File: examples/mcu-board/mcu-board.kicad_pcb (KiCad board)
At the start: 2 copper layers, 80 x 50 mm, 15 parts, among them J1 5V_IN, J2 PROG/IO, SW1 Reset, U1 MCU, U2 AMS1117-3.3

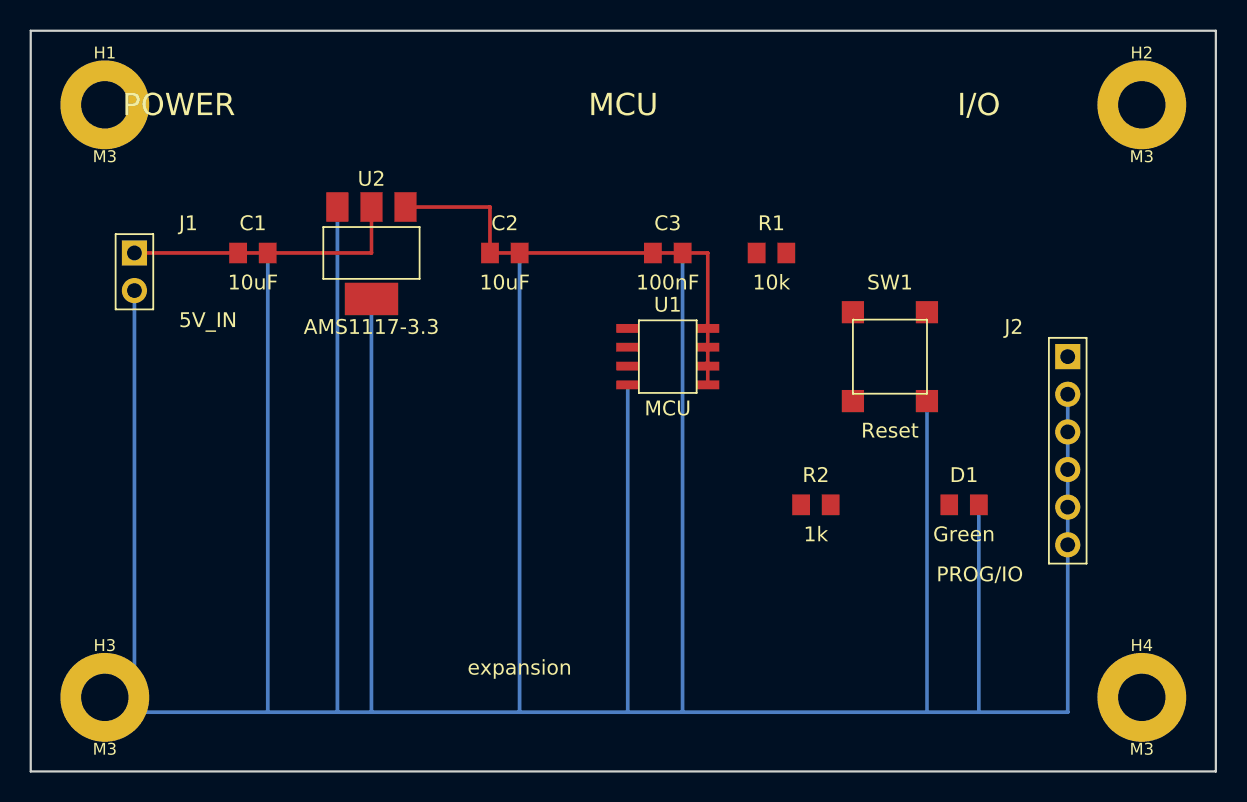
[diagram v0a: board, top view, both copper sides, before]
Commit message: examples/mcu-board: GND pour + silk relocation via kicad-mcp-pro
Two cleanups driven through the IPC API:

- Replace the manual fan of B.Cu GND tracks with a real copper zone
  fill spanning (91, 96)..(169, 144). pcb_refill_zones cuts proper
  thermal reliefs around the four mounting holes and the through-hole
  connector pads. The previous fan was a stand-in because kicad-cli
  can't compute zone fills offline; with KiCad GUI driving the fill
  via IPC we don't need the workaround any more.
- Move the "POWER" / "MCU" / "I/O" silkscreen labels off the y=100
  row (where they collided with the corner mounting holes' 6 mm pads)
  to y=104 between the holes and the component row. Size dropped
  1.5 mm → 1.2 mm to match the slightly tighter vertical band.

Workflow note: schematic edits run file-based via kicad-cli (no GUI
needed), but PCB edits go through KiCad's IPC API, which means KiCad
GUI must be open with the .kicad_pcb loaded and the API server
enabled (Preferences → Plugins → Enable plugin and API server).

Co-Authored-By: Claude Opus 4.7 (1M context) <noreply@anthropic.com>
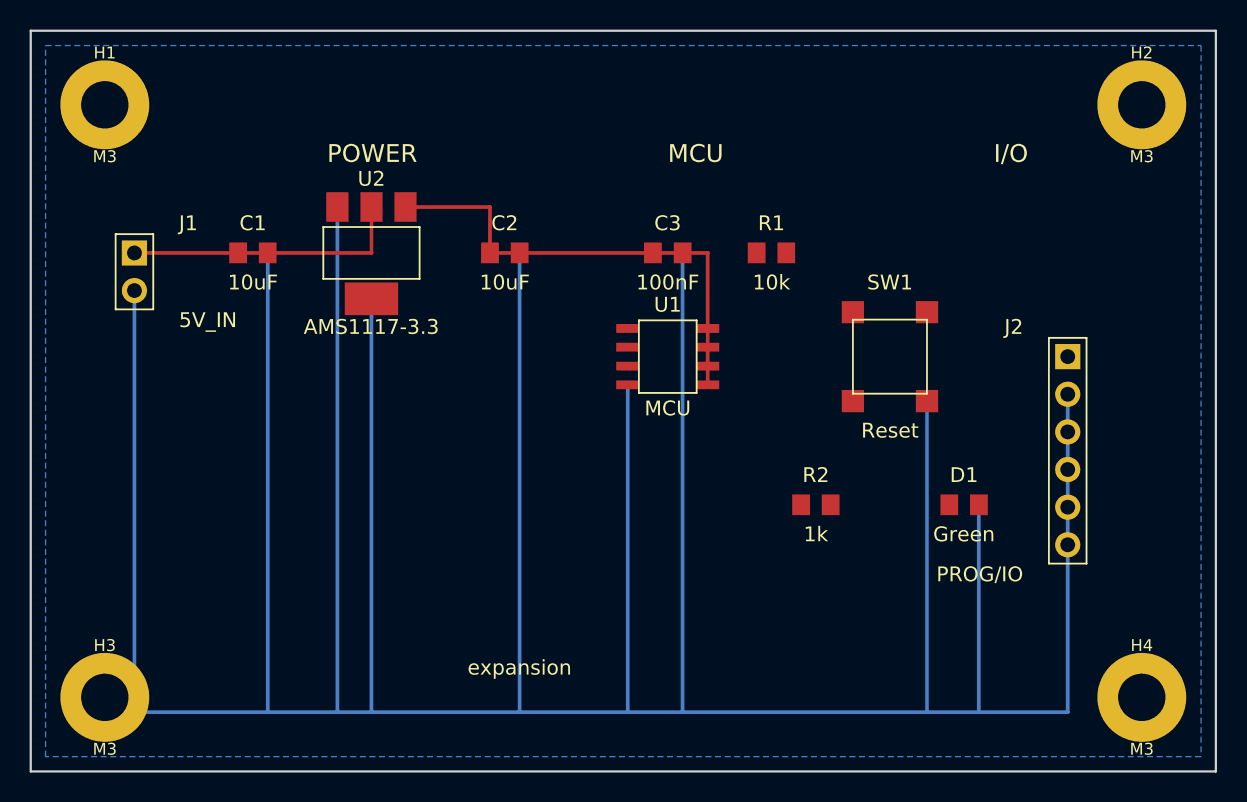
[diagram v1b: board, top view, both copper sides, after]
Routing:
- added copper zone on B.Cu, net GND
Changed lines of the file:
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@@
 	)
 	(gr_text "POWER"
-		(at 100 100 0)
+		(at 110 104 0)
 		(layer "F.SilkS")
 		(effects
 			(font
-				(size 1.5 1.5)
-				(thickness 0.25)
-			)
+				(size 1.2 1.2)
+				(line_spacing 0)
+			)
+			(justify left bottom)
 		)
 	)
 	(gr_text "MCU"
-		(at 130 100 0)
+		(at 133 104 0)
 		(layer "F.SilkS")
 		(effects
 			(font
-				(size 1.5 1.5)
-				(thickness 0.25)
-			)
+				(size 1.2 1.2)
+				(line_spacing 0)
+			)
+			(justify left bottom)
 		)
 	)
 	(gr_text "I/O"
-		(at 154 100 0)
+		(at 155 104 0)
 		(layer "F.SilkS")
 		(effects
 			(font
-				(size 1.5 1.5)
-				(thickness 0.25)
-			)
+				(size 1.2 1.2)
+				(line_spacing 0)
+			)
+			(justify left bottom)
 		)
 	)
@@
 		(net "+3V3")
 	)
+	(zone
+		(net "GND")
+		(layer "B.Cu")
+		(name "GND_pour")
+		(hatch edge 0.5)
+		(connect_pads
+			(clearance 0.3)
+		)
+		(min_thickness 0.25)
+		(fill yes
+			(thermal_gap 0.5)
+			(thermal_bridge_width 0.5)
+			(island_removal_mode 0)
+		)
+		(polygon
+			(pts
+				(xy 91 96) (xy 169 96) (xy 169 144) (xy 91 144)
+			)
+		)
+	)
 	(embedded_fonts no)

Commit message: examples/mcu-board: swap to system-library footprints
Replaces every inline footprint with a proper KiCad system-library
match — body silk, fab outline, courtyard, and pin-1 indicator now
travel with the part instead of being faked as separate board-level
shapes.

Workflow:
  - lib_assign_footprint to set the schematic Footprint property on
    each symbol (Package_SO:SOIC-8_3.9x4.9mm_P1.27mm,
    Package_TO_SOT_SMD:SOT-223-3_TabPin2,
    Capacitor_SMD:C_0805_2012Metric, etc.)
  - pcb_sync_from_schematic with replace_mismatched=True force=True to
    pull the new footprint definitions into the existing pads
  - delete the five board-level F.SilkS rectangles I had added as
    stand-in body outlines; the IPC-7351 footprints carry their own

Net coverage stays clean (100% pad coverage in the sync report).
ERC violations from the placeholder MCU symbol persist; they're
override-only for now and will get resolved when the schematic
symbols themselves are tightened.

Co-Authored-By: Claude Opus 4.7 (1M context) <noreply@anthropic.com>
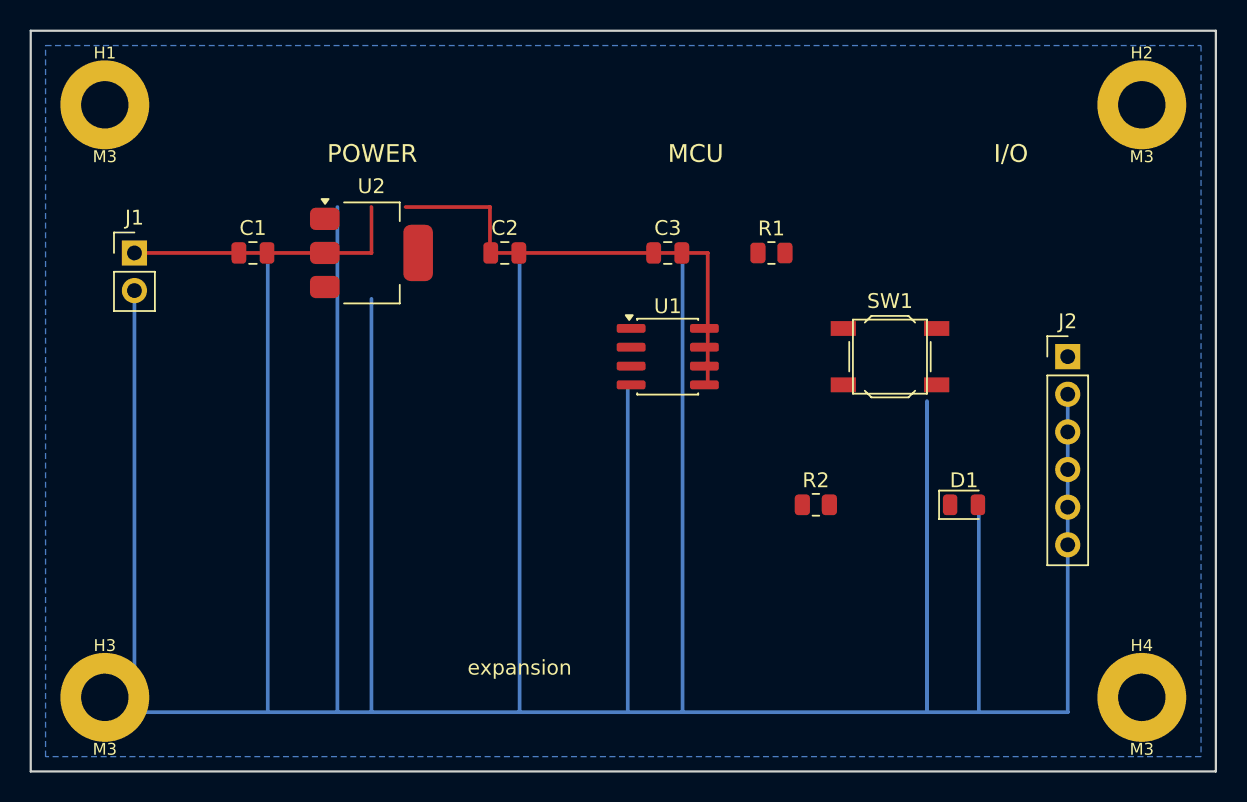
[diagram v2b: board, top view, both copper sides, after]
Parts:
- C1, C2, C3: footprint Resistor_SMD:C_0805_2012Metric -> C_0805_2012Metric
- D1: footprint Resistor_SMD:LED_0805_2012Metric -> LED_0805_2012Metric
- J1: footprint Connector_PinHeader_2.54mm:PinHeader_1x02 -> PinHeader_1x02_P2.54mm_Vertical
- J2: footprint Connector_PinHeader_2.54mm:PinHeader_1x06 -> PinHeader_1x06_P2.54mm_Vertical
- R1, R2: footprint Resistor_SMD:R_0805_2012Metric -> R_0805_2012Metric
- SW1: footprint Button_Switch_SMD:SW_SPST_TL3342 -> SW_SPST_TL3342
- U1: footprint Package_SO:SOIC-8_3.9x4.9mm_P1.27mm -> SOIC-8_3.9x4.9mm_P1.27mm
- U2: footprint Package_TO_SOT_SMD:SOT-223-3_TabPin2 -> SOT-223-3_TabPin2
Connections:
- net LED_A renamed /LED_A
- net PA1 renamed /PA1
- net PA2 renamed /PA2
- net PA3 renamed /PA3
- net PA5 renamed /PA5
- net RST renamed /RST
- C1 pad 1: VIN -> +5V
- D1 pad 1: PA4_OUT -> GND
- J1 pad 1: VIN -> +5V
- R2 pad 2: PA4_OUT -> GND
- U2 pad 2: VIN -> +3V3
- U2 pad 3: +3V3 -> +5V

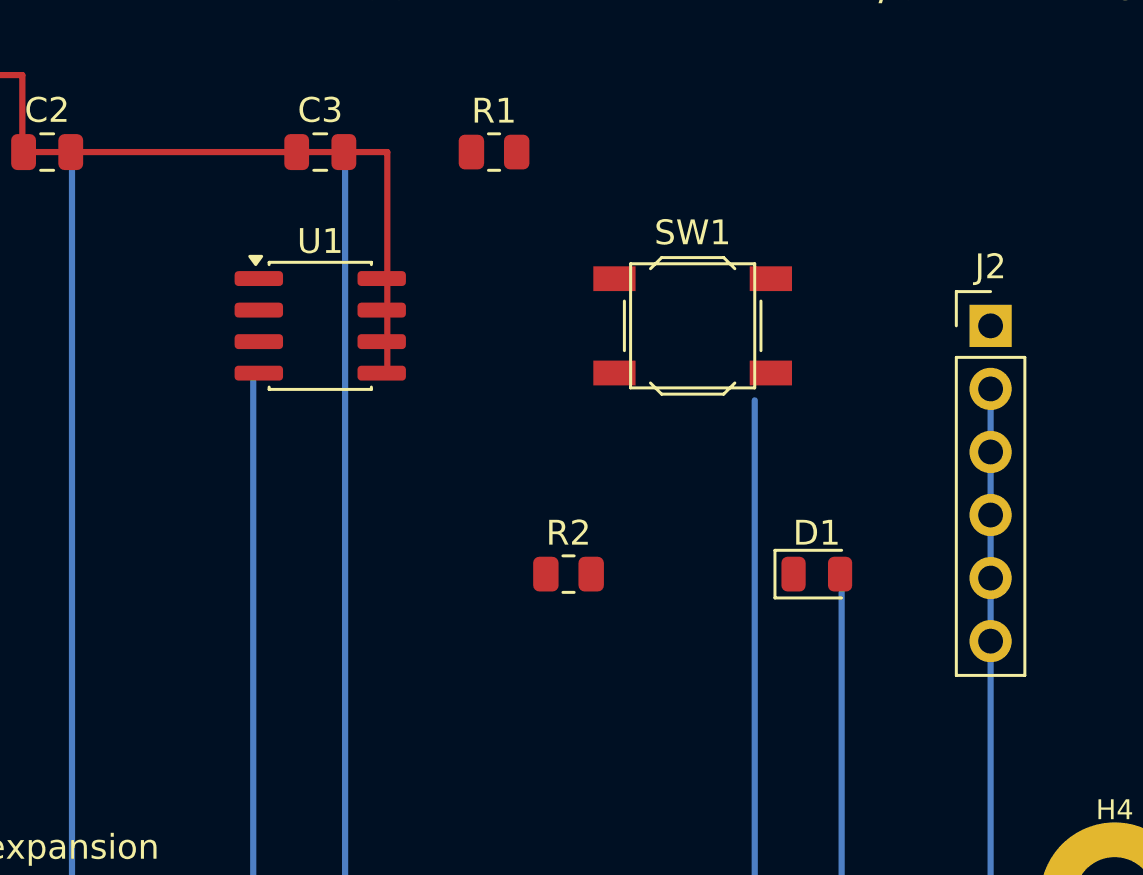
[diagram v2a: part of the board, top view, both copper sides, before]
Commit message: examples/mcu-board: route signal nets via kicad-mcp-pro
Manual routing pass to give the demo board real F.Cu / B.Cu traffic
beyond the existing power rails:

  RST    : U1.1 → R1.2 → SW1.1 → J2.3 (F.Cu, top lane at y=110/115.1)
  LED_A  : U1.7 → R2.1                (F.Cu, short L-shape)
  D1-K   : R2.2 → D1.A                (F.Cu, the LED chain anode hop)
  PA1    : U1.2 → J2.4                (F.Cu, above-MCU lane y=113,
                                       descends at x=158)
  PA2    : U1.3 → J2.5                (F.Cu stub → via at (126.5,
                                       117.635) → B.Cu under the GND
                                       pour, surfaces at J2.5; GND
                                       zone refilled to make the
                                       clearance pocket)
  PA3    : U1.6 → J2.6                (F.Cu, right-side detour around
                                       SW1 / R2 / D1 at y=122)

Routes were placed via route_single_track + pcb_add_via from MCP, then
saved with pcb_save and pcb_refill_zones. Freerouting headless wasn't
available (kicad-cli on this box doesn't expose Specctra DSN export),
so we did the routing by hand through MCP — which was the point of
this exercise anyway.

PA5 stays broken-out as a label only (no peripheral consumes it on
this board); it's available for the next iteration.

Co-Authored-By: Claude Opus 4.7 (1M context) <noreply@anthropic.com>
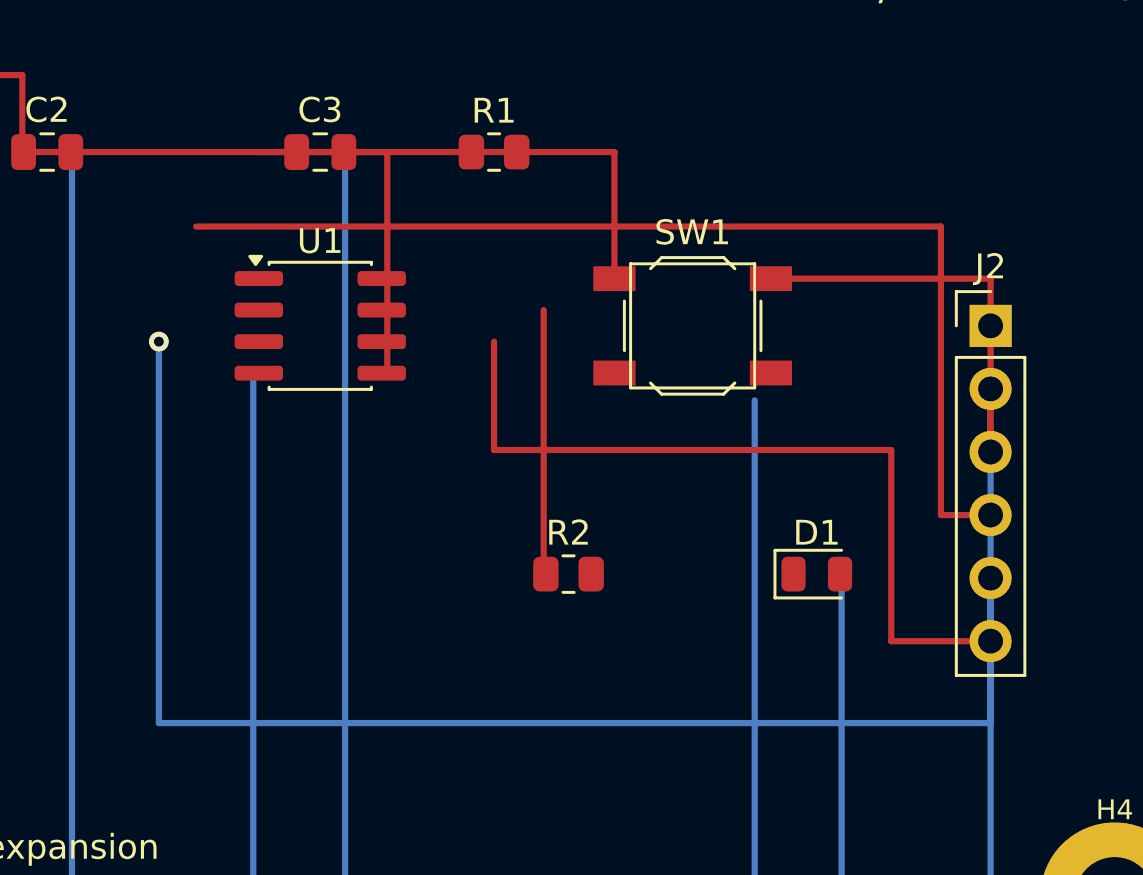
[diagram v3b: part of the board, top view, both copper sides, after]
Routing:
- net PA1: track 0.00 -> 43.6 mm
- net PA2: track 0.00 -> 39.3 mm
- net /LED_A: track 0.00 -> 38.7 mm
- net RST: track 0.00 -> 26.4 mm
- net GND: track 325.0 -> 340.4 mm, vias 0 -> 1
- net /RST: track 0.00 -> 8.85 mm
- net PA3: track 0.00 -> 4.00 mm
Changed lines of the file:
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@@
 		)
+	)
+	(via
+		(at 126.5 117.635)
+		(size 0.8)
+		(drill 0.4)
+		(layers "F.Cu" "B.Cu")
+		(net "GND")
 	)
 	(segment
@@
 	)
 	(segment
+		(start 126.5 117.635)
+		(end 126.5 133)
+		(width 0.25)
+		(layer "B.Cu")
+		(net "GND")
+	)
+	(segment
 		(start 115.3 106.9)
 		(end 121 106.9)
@@
 	)
 	(segment
+		(start 151.15 115.1)
+		(end 160 115.1)
+		(width 0.25)
+		(layer "F.Cu")
+		(net "/RST")
+	)
+	(segment
+		(start 140 117.635)
+		(end 140 122)
+		(width 0.25)
+		(layer "F.Cu")
+		(net "/LED_A")
+	)
+	(segment
+		(start 142 116.365)
+		(end 142 127)
+		(width 0.25)
+		(layer "F.Cu")
+		(net "/LED_A")
+	)
+	(segment
+		(start 140 122)
+		(end 156 122)
+		(width 0.25)
+		(layer "F.Cu")
+		(net "/LED_A")
+	)
+	(segment
+		(start 156 122)
+		(end 156 129.699999)
+		(width 0.25)
+		(layer "F.Cu")
+		(net "/LED_A")
+	)
+	(segment
 		(start 97 110)
 		(end 104 110)
@@
 		(net "VIN")
 	)
+	(segment
+		(start 160 115.1)
+		(end 160 122.08)
+		(width 0.25)
+		(layer "F.Cu")
+		(net "RST")
+	)
+	(segment
+		(start 144.85 110)
+		(end 144.85 115.1)
+		(width 0.25)
+		(layer "F.Cu")
+		(net "RST")
+	)
+	(segment
+		(start 140.9125 110)
+		(end 144.85 110)
+		(width 0.25)
+		(layer "F.Cu")
+		(net "RST")
+	)
+	(segment
+		(start 130.525 110)
+		(end 140.9125 110)
+		(width 0.25)
+		(layer "F.Cu")
+		(net "RST")
+	)
+	(segment
+		(start 158 113)
+		(end 158 124.62)
+		(width 0.25)
+		(layer "F.Cu")
+		(net "PA1")
+	)
+	(segment
+		(start 158 124.62)
+		(end 160 124.62)
+		(width 0.25)
+		(layer "F.Cu")
+		(net "PA1")
+	)
+	(segment
+		(start 128 113)
+		(end 158 113)
+		(width 0.25)
+		(layer "F.Cu")
+		(net "PA1")
+	)
+	(segment
+		(start 156 129.699999)
+		(end 160 129.699999)
+		(width 0.25)
+		(layer "F.Cu")
+		(net "PA3")
+	)
+	(segment
+		(start 160 133)
+		(end 160 127.16)
+		(width 0.25)
+		(layer "B.Cu")
+		(net "PA2")
+	)
+	(segment
+		(start 126.5 133)
+		(end 160 133)
+		(width 0.25)
+		(layer "B.Cu")
+		(net "PA2")
+	)
 	(zone

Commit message: examples/mcu-board: replan layout, route power; prep gemini-cli handoff
Layout pass driven by user feedback ("don't route in straight lines",
"think about routing first then place components", "headers/switch on
edges, MCU at the centre"):

  - U1 (MCU) moved to the board centre at (130, 120).
  - J1 (5V_IN) on the left edge (95, 120), J2 (PROG/IO) on the right
    edge (165, 114), SW1 (Reset) on the bottom-right edge (150, 138).
  - C1 / C2 / C3 rotated 90° (vertical) so the main F.Cu rails can
    run horizontally with single-pad stubs instead of crossing both
    pads (the earlier mistake that shorted +5V to GND through the cap
    body).
  - C3 moved adjacent to U1's VCC pin at (135, 123) for proper
    decoupling instead of sitting 7 mm away.
  - R1 rotated 90° and moved to (124, 117) so its RST pad sits a
    single 45° hop from U1.1.
  - Bottom strip (y > 130) deliberately left empty for additional
    peripherals — `expansion` silk text already there.

Routing — first pass via a kicad-mcp-pro sub-agent:
  - VIN ("+5V" net per the schematic) wired J1.1 → C1.1 → U2.3 with
    a 45° kink at the LDO entry. 6 segments.
  - +3V3 wired U2.tab → C2.1 → R1.1 → U1.5 → C3.1 with 45° corners
    around U1. 15 segments.
  - GND copper pour (B.Cu) refilled around the new component
    positions; thermal reliefs reform automatically.

Stale traces from earlier rounds were deleted (orphan VIN segment
that shorted +5V↔VIN, +3V3 trace that grazed U1.6/PA3, etc.).

Workflow + gemini-cli handoff:
  - .mcp.json now also lists kicad-mcp-pro under the alias `gemini`,
    matching how the user wants to address it from gemini-cli.
  - Added .gemini/settings.json — gemini-cli reads its mcpServers
    block from `.gemini/settings.json` (project) or `~/.gemini/...`
    (user); a `.mcp.json` alone is invisible to it.
  - Note for whoever picks this up: KiCad's IPC API only accepts one
    client at a time, so don't drive PCB edits from this Claude Code
    session and gemini-cli simulta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
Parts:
- moved SW1 21.1 mm to (150.0, 138.0)
- moved R1 17.5 mm to (124.0, 117.0)
- moved C3 13.2 mm to (135.0, 123.0)
- moved C1 10.4 mm to (102.0, 120.0)
- moved C2 10.2 mm to (120.0, 120.0)
- moved J1 10.2 mm to (95.0, 120.0)
- moved U2 10.2 mm to (111.0, 120.0)
- moved J2 5.83 mm to (165.0, 114.0)
- moved D1 5.10 mm to (148.0, 128.0)
- moved U1 4.24 mm to (130.0, 120.0)
- moved R2 3.16 mm to (140.0, 128.0)
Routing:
- net GND: track 340.4 -> 0.00 mm, vias 1 -> 0
- net /RST: track 8.85 -> 67.0 mm
- net PA1: track 43.6 -> 0.00 mm
- net PA2: track 39.3 -> 0.00 mm
- net /LED_A: track 38.7 -> 0.00 mm
- net RST: track 26.4 -> 0.00 mm
- net VIN: track 19.1 -> 0.00 mm
- net +5V: track 0.00 -> 14.8 mm
- net PA3: track 4.00 -> 0.00 mm
